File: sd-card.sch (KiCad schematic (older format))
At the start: 9 parts

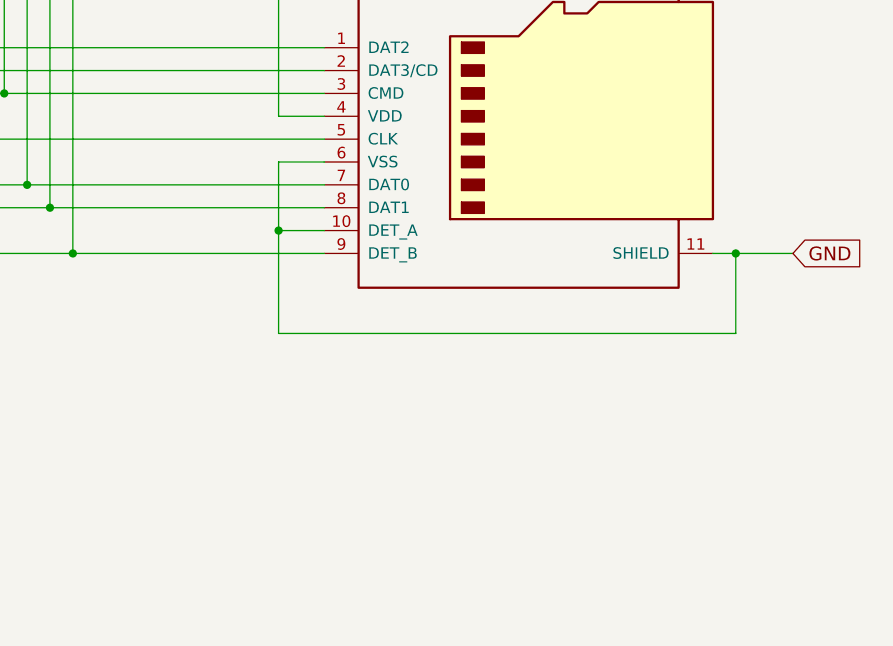
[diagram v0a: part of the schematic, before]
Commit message: feature complete; the next step is the verification of the values and the schematics
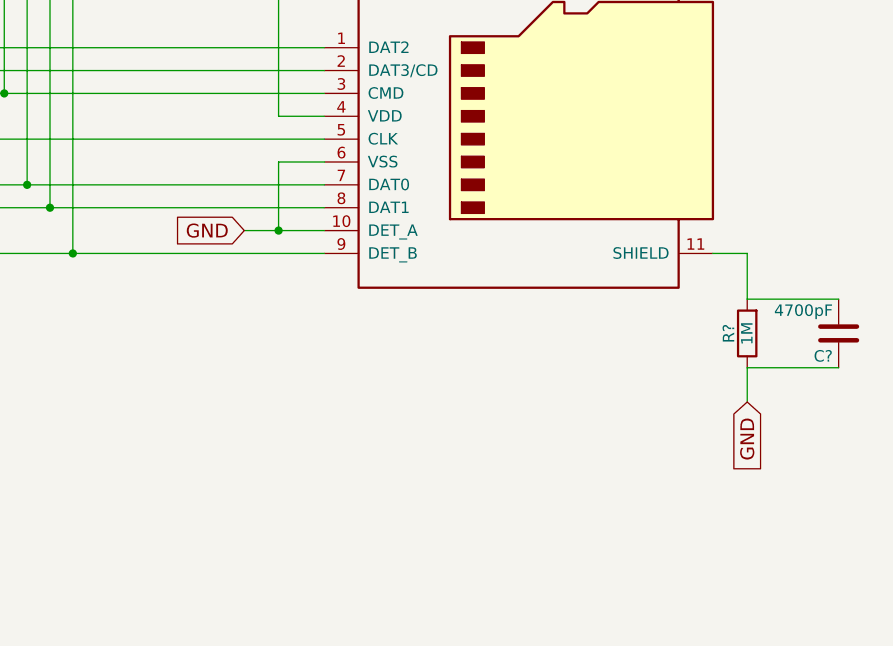
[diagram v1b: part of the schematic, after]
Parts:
- added C?: 4700pF, symbol C
- added R?: 1M, symbol R
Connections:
- net GND: now also C?.1, R?.1; no longer J?.11 (SHIELD)
- new net: C?.2, J?.11 (SHIELD), R?.2
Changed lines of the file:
@@
 	8650 3400 8450 3400
 Wire Wire Line
-	8450 3400 8450 4150
-Wire Wire Line
-	8450 3700 8650 3700
+	8300 3700 8650 3700
 Connection ~ 8450 3700
 $Comp
@@
 Wire Notes Line
 	2000 5950 2000 3950
-Connection ~ 10450 3800
-Text GLabel 10700 3800 2    60   Input ~ 0
+Text GLabel 8300 3700 0    60   Input ~ 0
 GND
 Wire Wire Line
-	10350 3800 10700 3800
+	8450 3400 8450 3700
+Text GLabel 10500 4450 3    60   Input ~ 0
+GND
+$Comp
+L C C?
+U 1 1 59A52C88
+P 10900 4150
+F 0 "C?" H 10925 4250 50  0000 L CNN
+F 1 "4700pF" H 10925 4050 50  0000 L CNN
+F 2 "" H 10938 4000 50  0001 C CNN
+F 3 "" H 10900 4150 50  0001 C CNN
+	1    10900 4150
+	-1   0    0    1
+$EndComp
+$Comp
+L R R?
+U 1 1 59A52C8F
+P 10500 4150
+F 0 "R?" V 10580 4150 50  0000 C CNN
+F 1 "1M" V 10500 4150 50  0000 C CNN
+F 2 "" V 10430 4150 50  0001 C CNN
+F 3 "" H 10500 4150 50  0001 C CNN
+	1    10500 4150
+	-1   0    0    1
+$EndComp
 Wire Wire Line
-	10450 4150 10450 3800
+	10500 4450 10500 4300
 Wire Wire Line
-	8450 4150 10450 4150
+	10500 4300 10900 4300
+Wire Wire Line
+	10500 4000 10900 4000
+Wire Wire Line
+	10500 4000 10500 3800
+Wire Wire Line
+	10500 3800 10350 3800
 $EndSCHEMATC

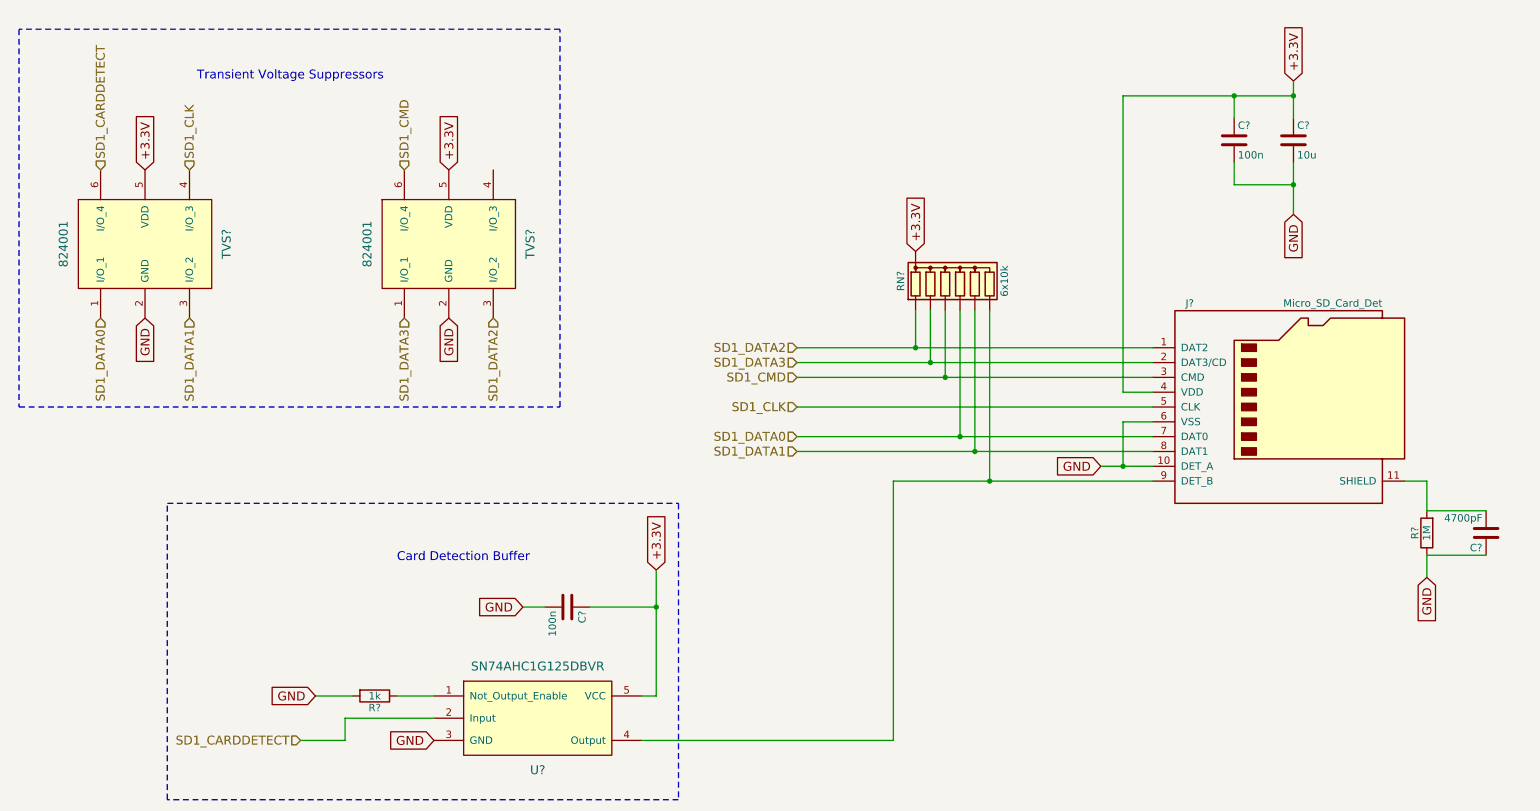
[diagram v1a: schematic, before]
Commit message: this version contains the datasheets and the footprints of the parts
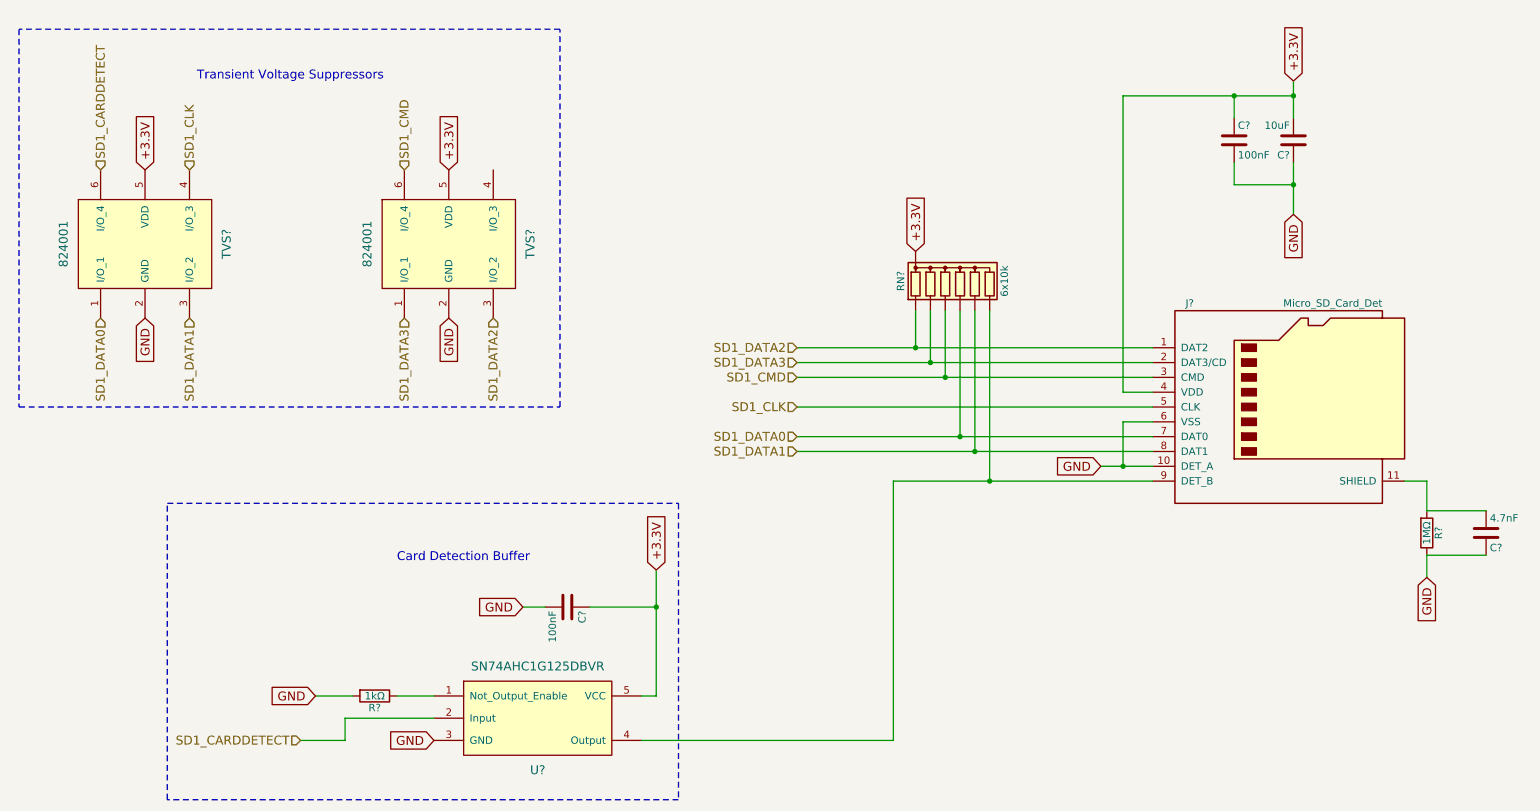
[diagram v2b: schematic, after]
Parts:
- removed C?: 10u, symbol C
- removed C? (x2): 100n, symbol C
- removed C?: 4700pF, symbol C
- removed R?: 1k, symbol R
- removed R?: 1M, symbol R
- added C?: 10uF, Capacitors_SMD:C_0603_HandSoldering, symbol C
- added C? (x2): 100nF, Capacitors_SMD:C_0603_HandSoldering, symbol C
- added C?: 4.7nF, Capacitors_SMD:C_0603_HandSoldering, symbol C
- added R?: 1MΩ, Resistors_SMD:R_0603_HandSoldering, symbol R
- added R?: 1kΩ, Resistors_SMD:R_0603_HandSoldering, symbol R
- J?: footprint (none) -> Connectors_Hirose:microSD_Card_Receptacle_Hirose_DM3AT-SF-PEJM5
- TVS? (x2): footprint (none) -> Housings_SOT-23_SOT-143_TSOT-6:SOT-23-6
- U?: footprint (none) -> Housings_SOT-23_SOT-143_TSOT-6:SOT-23-5
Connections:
- net +3.3V: now also C?.1, C?.1, C?.2
- net GND: now also C?.1, C?.1, C?.2, C?.2, R?.1, R?.2
- net at J?.11 (SHIELD): now also C?.2, R?.2
- net at U?.1 (Not_Output_Enable): now also R?.1
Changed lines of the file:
@@
 F 0 "J?" H 8900 4000 50  0000 C CNN
 F 1 "Micro_SD_Card_Det" H 10200 4000 50  0000 R CNN
-F 2 "" H 11600 4000 50  0001 C CNN
+F 2 "Connectors_Hirose:microSD_Card_Receptacle_Hirose_DM3AT-SF-PEJM5" H 11600 4000 50  0001 C CNN
 F 3 "http://hu.farnell.com/wurth-elektronik/693071010811/connector-micro-sd-smt-r-a-8way/dp/2081363" H 9550 3400 50  0001 C CNN
 	1    9550 3300
@@
 Wire Wire Line
 	9600 1100 9600 1350
-$Comp
-L C C?
-U 1 1 59A17CEA
-P 9600 1500
-F 0 "C?" H 9625 1600 50  0000 L CNN
-F 1 "10u" H 9625 1400 50  0000 L CNN
-F 2 "" H 9638 1350 50  0001 C CNN
-F 3 "" H 9600 1500 50  0001 C CNN
-	1    9600 1500
-	1    0    0    -1
-$EndComp
-$Comp
-L C C?
-U 1 1 59A17D15
-P 9200 1500
-F 0 "C?" H 9225 1600 50  0000 L CNN
-F 1 "100n" H 9225 1400 50  0000 L CNN
-F 2 "" H 9238 1350 50  0001 C CNN
-F 3 "" H 9200 1500 50  0001 C CNN
-	1    9200 1500
-	1    0    0    -1
-$EndComp
 Connection ~ 9600 1200
 Wire Wire Line
@@
 F 0 "TVS?" V 2400 2100 60  0000 C CNN
 F 1 "824001" V 1300 2100 60  0000 C CNN
-F 2 "" H 2700 2150 60  0001 C CNN
+F 2 "Housings_SOT-23_SOT-143_TSOT-6:SOT-23-6" H 2700 2150 60  0001 C CNN
 F 3 "http://hu.farnell.com/wurth-elektronik/824001/diode-array-tvs/dp/1748613" H 2700 2150 60  0001 C CNN
 	1    2700 2150
@@
 F 0 "TVS?" V 4450 2100 60  0000 C CNN
 F 1 "824001" V 3350 2100 60  0000 C CNN
-F 2 "" H 4750 2150 60  0001 C CNN
+F 2 "Housings_SOT-23_SOT-143_TSOT-6:SOT-23-6" H 4750 2150 60  0001 C CNN
 F 3 "http://hu.farnell.com/wurth-elektronik/824001/diode-array-tvs/dp/1748613" H 4750 2150 60  0001 C CNN
 	1    4750 2150
@@
 F 0 "U?" H 4500 4450 60  0000 C CNN
 F 1 "SN74AHC1G125DBVR" H 4500 5150 60  0000 C CNN
-F 2 "" H 4450 5100 60  0001 C CNN
-F 3 "" H 4450 5100 60  0001 C CNN
+F 2 "Housings_SOT-23_SOT-143_TSOT-6:SOT-23-5" H 4450 5100 60  0001 C CNN
+F 3 "hu.farnell.com/texas-instruments/sn74ahc1g125dbvt/ic-sm-logic-74ahc1g-buffer/dp/1607808" H 4450 5100 60  0001 C CNN
 	1    4450 5100
 	1    0    0    -1
@@
 Text GLabel 3000 5250 0    60   Input ~ 0
 GND
-$Comp
-L R R?
-U 1 1 59A1A304
-P 3400 5250
-F 0 "R?" V 3480 5250 50  0000 C CNN
-F 1 "1k" V 3400 5250 50  0000 C CNN
-F 2 "" V 3330 5250 50  0001 C CNN
-F 3 "" H 3400 5250 50  0001 C CNN
-	1    3400 5250
-	0    1    1    0
-$EndComp
 Wire Wire Line
 	3000 5250 3250 5250
@@
 Text GLabel 4400 4650 0    60   Input ~ 0
 GND
-$Comp
-L C C?
-U 1 1 59A1AED2
-P 4700 4650
-F 0 "C?" H 4725 4750 50  0000 L CNN
-F 1 "100n" H 4725 4550 50  0000 L CNN
-F 2 "" H 4738 4500 50  0001 C CNN
-F 3 "" H 4700 4650 50  0001 C CNN
-	1    4700 4650
-	0    1    1    0
-$EndComp
 Wire Wire Line
 	5300 4650 4850 4650
@@
 Text GLabel 10500 4450 3    60   Input ~ 0
 GND
-$Comp
-L C C?
-U 1 1 59A52C88
+Wire Wire Line
+	10500 4450 10500 4300
+Wire Wire Line
+	10500 4300 10900 4300
+Wire Wire Line
+	10500 4000 10900 4000
+Wire Wire Line
+	10500 4000 10500 3800
+Wire Wire Line
+	10500 3800 10350 3800
+$Comp
+L R R?
+U 1 1 59A82701
+P 3400 5250
+F 0 "R?" V 3480 5250 50  0000 C CNN
+F 1 "1kΩ" V 3400 5250 50  0000 C CNN
+F 2 "Resistors_SMD:R_0603_HandSoldering" V 3330 5250 30  0001 C CNN
+F 3 "hu.farnell.com/multicomp/mcmr06x1001ftl/res-ceramic-1k-1-0-1w-0603/dp/2073348" H 3400 5250 30  0001 C CNN
+	1    3400 5250
+	0    1    1    0
+$EndComp
+$Comp
+L C C?
+U 1 1 59A66C23
+P 9600 1500
+F 0 "C?" H 9625 1600 50  0000 L CNN
+F 1 "10uF" H 9625 1400 50  0000 L CNN
+F 2 "Capacitors_SMD:C_0603_HandSoldering" H 9638 1350 30  0001 C CNN
+F 3 "http://hu.farnell.com/murata/grm188r60g106me47d/cap-mlcc-x5r-10uf-4v-0603/dp/2688517" H 9600 1500 60  0001 C CNN
+F 4 "http://hu.farnell.com/avx/06036d106mat2a/cap-mlcc-x5r-10uf-6-3v-0603/dp/1833804" H 9600 1500 60  0001 C CNN "avx"
+	1    9600 1500
+	-1   0    0    1
+$EndComp
+$Comp
+L C C?
+U 1 1 59A672EC
+P 9200 1500
+F 0 "C?" H 9225 1600 50  0000 L CNN
+F 1 "100nF" H 9225 1400 50  0000 L CNN
+F 2 "Capacitors_SMD:C_0603_HandSoldering" H 9238 1350 30  0001 C CNN
+F 3 "hu.farnell.com/avx/06035c104kat2a/cap-mlcc-x7r-100nf-50v-0603/dp/1301804" H 9200 1500 60  0001 C CNN
+	1    9200 1500
+	1    0    0    -1
+$EndComp
+$Comp
+L C C?
+U 1 1 59A67859
+P 4700 4650
+F 0 "C?" H 4725 4750 50  0000 L CNN
+F 1 "100nF" H 4725 4550 50  0000 L CNN
+F 2 "Capacitors_SMD:C_0603_HandSoldering" H 4738 4500 30  0001 C CNN
+F 3 "hu.farnell.com/avx/06035c104kat2a/cap-mlcc-x7r-100nf-50v-0603/dp/1301804" H 4700 4650 60  0001 C CNN
+	1    4700 4650
+	0    1    1    0
+$EndComp
+$Comp
+L R R?
+U 1 1 59A6A008
+P 10500 4150
+F 0 "R?" V 10580 4150 50  0000 C CNN
+F 1 "1MΩ" V 10500 4150 50  0000 C CNN
+F 2 "Resistors_SMD:R_0603_HandSoldering" V 10430 4150 50  0001 C CNN
+F 3 "http://hu.farnell.com/multicomp/mcwr06x1004ftl/res-thick-film-1m-1-0-1w-0603/dp/2447285" H 10500 4150 50  0001 C CNN
+	1    10500 4150
+	1    0    0    1
+$EndComp
+$Comp
+L C C?
+U 1 1 59A6A959
 P 10900 4150
 F 0 "C?" H 10925 4250 50  0000 L CNN
-F 1 "4700pF" H 10925 4050 50  0000 L CNN
-F 2 "" H 10938 4000 50  0001 C CNN
-F 3 "" H 10900 4150 50  0001 C CNN
+F 1 "4.7nF" H 10925 4050 50  0000 L CNN
+F 2 "Capacitors_SMD:C_0603_HandSoldering" H 10938 4000 50  0001 C CNN
+F 3 "http://hu.farnell.com/avx/06035c472kat2a/cap-mlcc-x7r-4-7nf-50v-0603/dp/317263" H 10900 4150 50  0001 C CNN
 	1    10900 4150
-	-1   0    0    1
-$EndComp
-$Comp
-L R R?
-U 1 1 59A52C8F
-P 10500 4150
-F 0 "R?" V 10580 4150 50  0000 C CNN
-F 1 "1M" V 10500 4150 50  0000 C CNN
-F 2 "" V 10430 4150 50  0001 C CNN
-F 3 "" H 10500 4150 50  0001 C CNN
-	1    10500 4150
-	-1   0    0    1
-$EndComp
-Wire Wire Line
-	10500 4450 10500 4300
-Wire Wire Line
-	10500 4300 10900 4300
-Wire Wire Line
-	10500 4000 10900 4000
-Wire Wire Line
-	10500 4000 10500 3800
-Wire Wire Line
-	10500 3800 10350 3800
+	1    0    0    1
+$EndComp
 $EndSCHEMATC

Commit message: some issues fixed by the bugfixer; formal verification needed
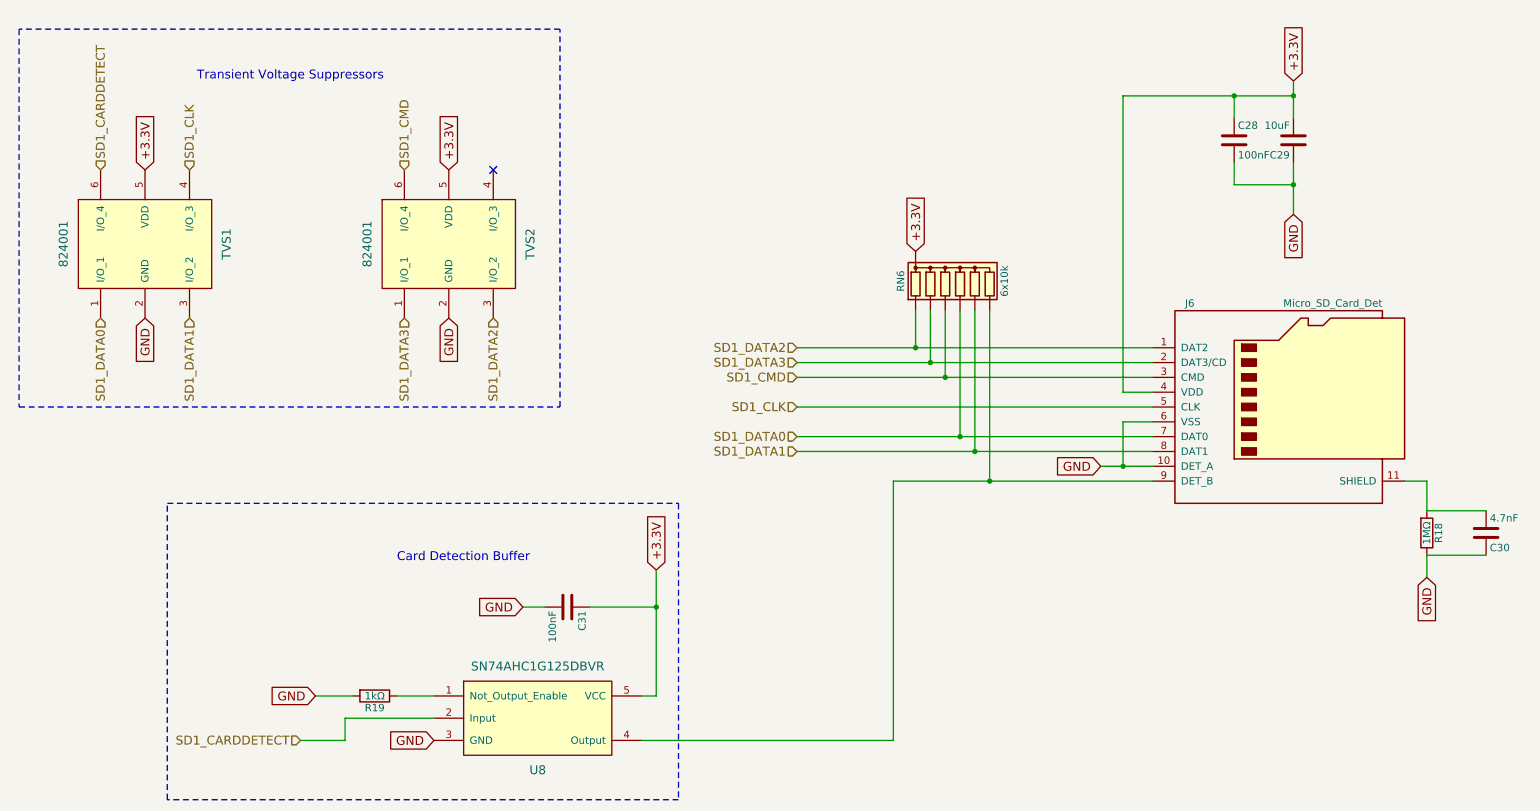
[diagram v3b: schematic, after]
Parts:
- gave numbers to parts that had none: 11
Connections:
- no-connect marks 0 -> 1
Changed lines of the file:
@@
 $EndDescr
 $Comp
-L Micro_SD_Card_Det J?
+L Micro_SD_Card_Det J6
 U 1 1 599FE4CA
 P 9550 3300
-F 0 "J?" H 8900 4000 50  0000 C CNN
+F 0 "J6" H 8900 4000 50  0000 C CNN
 F 1 "Micro_SD_Card_Det" H 10200 4000 50  0000 R CNN
 F 2 "Connectors_Hirose:microSD_Card_Receptacle_Hirose_DM3AT-SF-PEJM5" H 11600 4000 50  0001 C CNN
@@
 	6250 3600 8650 3600
 $Comp
-L R_Network06 RN?
+L R_Network06 RN6
 U 1 1 59A16EDB
 P 7350 2450
-F 0 "RN?" V 6950 2450 50  0000 C CNN
+F 0 "RN6" V 6950 2450 50  0000 C CNN
 F 1 "6x10k" V 7650 2450 50  0000 C CNN
 F 2 "Resistors_THT:R_Array_SIP7" V 7725 2450 50  0001 C CNN
@@
 Connection ~ 8450 3700
 $Comp
-L 824001 TVS?
+L 824001 TVS1
 U 1 1 59A17330
 P 2700 2150
-F 0 "TVS?" V 2400 2100 60  0000 C CNN
+F 0 "TVS1" V 2400 2100 60  0000 C CNN
 F 1 "824001" V 1300 2100 60  0000 C CNN
 F 2 "Housings_SOT-23_SOT-143_TSOT-6:SOT-23-6" H 2700 2150 60  0001 C CNN
@@
 $EndComp
 $Comp
-L 824001 TVS?
+L 824001 TVS2
 U 1 1 59A17379
 P 4750 2150
-F 0 "TVS?" V 4450 2100 60  0000 C CNN
+F 0 "TVS2" V 4450 2100 60  0000 C CNN
 F 1 "824001" V 3350 2100 60  0000 C CNN
 F 2 "Housings_SOT-23_SOT-143_TSOT-6:SOT-23-6" H 4750 2150 60  0001 C CNN
@@
 SD1_CARDDETECT
 $Comp
-L SN74AHC1G125DBVR U?
+L SN74AHC1G125DBVR U8
 U 1 1 59A18CB9
 P 4450 5100
-F 0 "U?" H 4500 4450 60  0000 C CNN
+F 0 "U8" H 4500 4450 60  0000 C CNN
 F 1 "SN74AHC1G125DBVR" H 4500 5150 60  0000 C CNN
 F 2 "Housings_SOT-23_SOT-143_TSOT-6:SOT-23-5" H 4450 5100 60  0001 C CNN
@@
 	10500 3800 10350 3800
 $Comp
-L R R?
+L R R19
 U 1 1 59A82701
 P 3400 5250
-F 0 "R?" V 3480 5250 50  0000 C CNN
+F 0 "R19" V 3480 5250 50  0000 C CNN
 F 1 "1kΩ" V 3400 5250 50  0000 C CNN
 F 2 "Resistors_SMD:R_0603_HandSoldering" V 3330 5250 30  0001 C CNN
@@
 $EndComp
 $Comp
-L C C?
+L C C29
 U 1 1 59A66C23
 P 9600 1500
-F 0 "C?" H 9625 1600 50  0000 L CNN
+F 0 "C29" H 9625 1600 50  0000 L CNN
 F 1 "10uF" H 9625 1400 50  0000 L CNN
 F 2 "Capacitors_SMD:C_0603_HandSoldering" H 9638 1350 30  0001 C CNN
@@
 $EndComp
 $Comp
-L C C?
+L C C28
 U 1 1 59A672EC
 P 9200 1500
-F 0 "C?" H 9225 1600 50  0000 L CNN
+F 0 "C28" H 9225 1600 50  0000 L CNN
 F 1 "100nF" H 9225 1400 50  0000 L CNN
 F 2 "Capacitors_SMD:C_0603_HandSoldering" H 9238 1350 30  0001 C CNN
@@
 $EndComp
 $Comp
-L C C?
+L C C31
 U 1 1 59A67859
 P 4700 4650
-F 0 "C?" H 4725 4750 50  0000 L CNN
+F 0 "C31" H 4725 4750 50  0000 L CNN
 F 1 "100nF" H 4725 4550 50  0000 L CNN
 F 2 "Capacitors_SMD:C_0603_HandSoldering" H 4738 4500 30  0001 C CNN
@@
 $EndComp
 $Comp
-L R R?
+L R R18
 U 1 1 59A6A008
 P 10500 4150
-F 0 "R?" V 10580 4150 50  0000 C CNN
+F 0 "R18" V 10580 4150 50  0000 C CNN
 F 1 "1MΩ" V 10500 4150 50  0000 C CNN
 F 2 "Resistors_SMD:R_0603_HandSoldering" V 10430 4150 50  0001 C CNN
@@
 $EndComp
 $Comp
-L C C?
+L C C30
 U 1 1 59A6A959
 P 10900 4150
-F 0 "C?" H 10925 4250 50  0000 L CNN
+F 0 "C30" H 10925 4250 50  0000 L CNN
 F 1 "4.7nF" H 10925 4050 50  0000 L CNN
 F 2 "Capacitors_SMD:C_0603_HandSoldering" H 10938 4000 50  0001 C CNN
@@
 	1    0    0    1
 $EndComp
+NoConn ~ 4200 1700
 $EndSCHEMATC
